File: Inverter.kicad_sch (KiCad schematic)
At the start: 53 parts, among them IC1 STGIPQ3H60T-HL, IC2 ACS724LLCTR-05AU-T

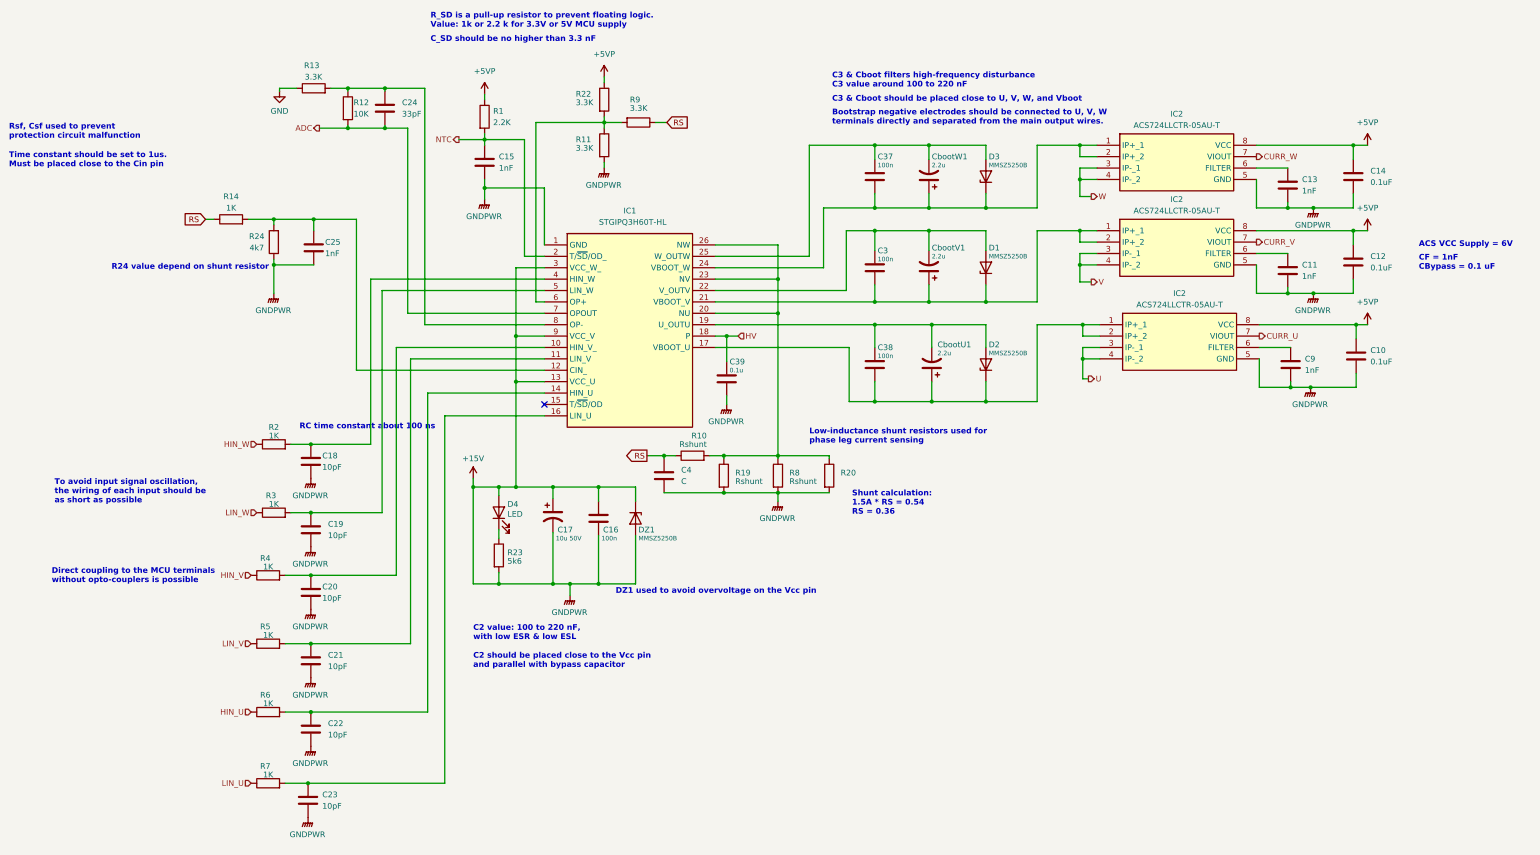
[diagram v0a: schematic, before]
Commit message: add overcurrent protection
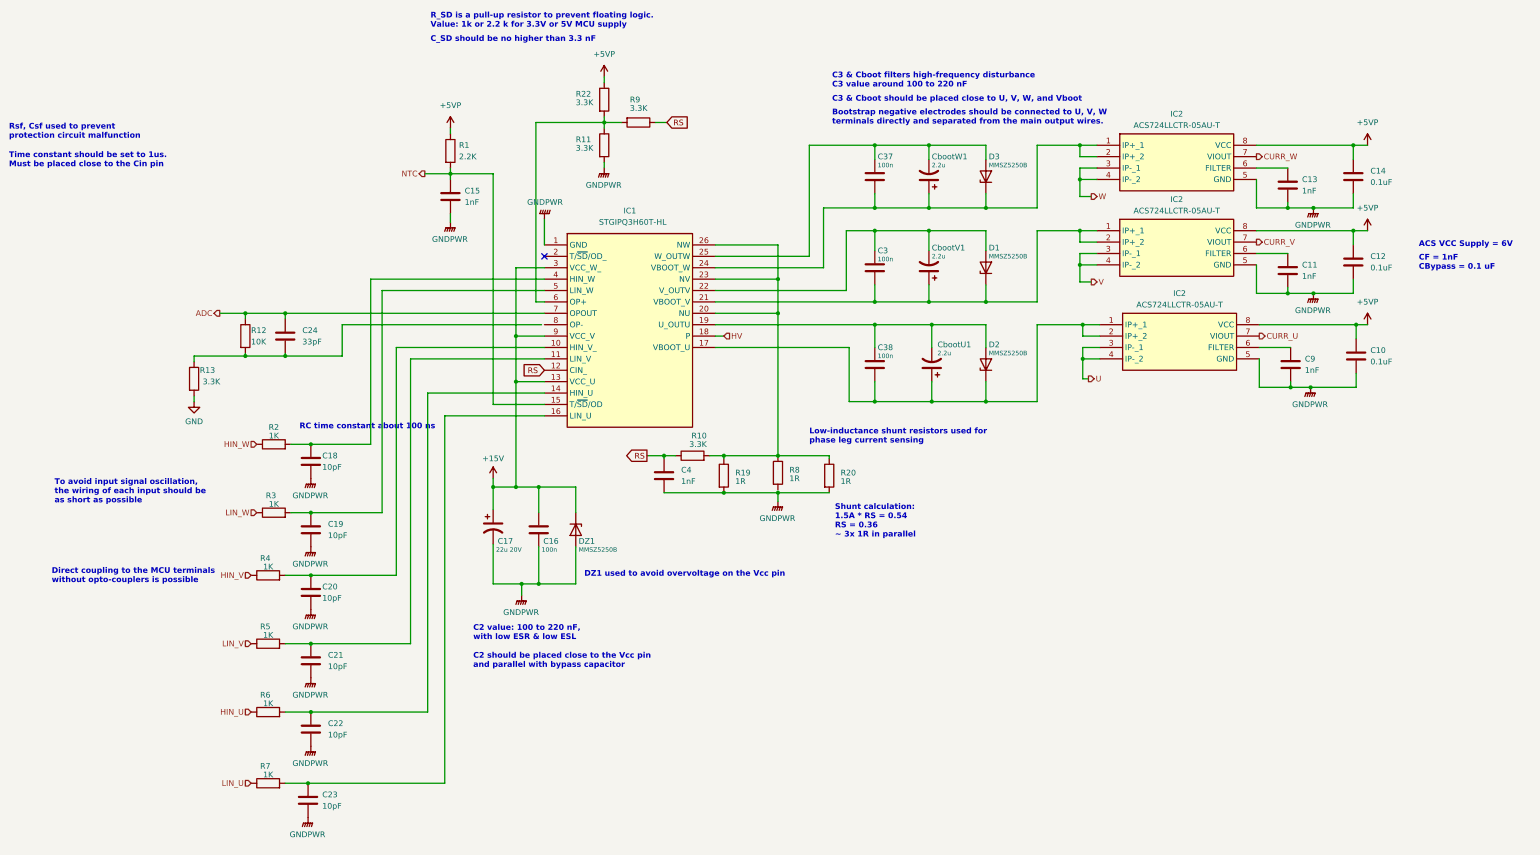
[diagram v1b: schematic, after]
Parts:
- removed C25: 1nF, symbol Device:C
- removed C39: 0.1u, symbol Device:C
- removed D4: LED, LED_THT:LED_D5.0mm, symbol Device:LED
- removed R14: 1K, Resistor_THT:R_Axial_DIN0309_L9.0mm_D3.2mm_P12.70mm_Horizontal, symbol Device:R
- removed R23: 5k6, Resistor_THT:R_Axial_DIN0309_L9.0mm_D3.2mm_P12.70mm_Horizontal, symbol Device:R
- removed R24: 4k7, Resistor_THT:R_Axial_DIN0309_L9.0mm_D3.2mm_P12.70mm_Horizontal, symbol Device:R
- C17: value 10u 50V -> 22u 20V
- C4: value C -> 1nF
- R10: value Rshunt -> 3.3K
- R19, R20, R8: value Rshunt -> 1R
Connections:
- net +15V: no longer C10.1, C11.1, C12.1, C13.1, C14.1, C15.2, C16.1, C17.2, C18.2, C19.2, C20.2, C21.2, C22.2, C23.2, C4.2, C9.1, DZ1.2 (A), IC1.1 (GND), IC2.5 (GND), IC2.5 (GND), IC2.5 (GND), R11.2, R19.2, R20.2, R8.2
- net ADC: now also C24.1, R12.1; no longer C24.2, R12.2
- net GND: now also R13.2; no longer R13.1
- net NTC: now also IC1.15 (T/~{SD}/OD); no longer IC1.2 (T/~{SD}/OD_)
- net RS: now also IC1.12 (CIN_)
- new net: C24.2, R12.2, R13.1
- new net GNDPWR: C10.1, C11.1, C12.1, C13.1, C14.1, C15.2, C16.1, C17.2, C18.2, C19.2, C20.2, C21.2, C22.2, C23.2, C4.2, C9.1, DZ1.2 (A), IC1.1 (GND), IC2.5 (GND), IC2.5 (GND), IC2.5 (GND), R11.2, R19.2, R20.2
- now unconnected: IC1.8 (OP-)
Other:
- note added: "Shunt calculation: 1.5A * RS = 0.54 RS = 0.36 ~ 3x 1R in parallel"
- note removed: "R24 value depend on shunt resistor"
- note removed: "Shunt calculation: 1.5A * RS = 0.54 RS = 0.36"
- moved on the sheet: C15, C16, C17, C24, DZ1, R1, R12, R13

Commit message: update schematics
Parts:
- removed C16: 100n, symbol Device:C
- removed C17: 22u 20V, symbol Device:C_Polarized_US
- removed DZ1: MMSZ5250B, symbol Device:D_Zener
- C10, C11, C12, C13, C14, C15, C18, C19, C20, C21, C22, C23, C24, C3, C37, C38, C4, C9: footprint (none) -> Capacitor_THT:C_Disc_D4.3mm_W1.9mm_P5.00mm
- CbootU1, CbootV1, CbootW1: footprint (none) -> Capacitor_THT:CP_Radial_D5.0mm_P2.50mm
- D1, D2, D3: footprint (none) -> Diode_THT:D_A-405_P7.62mm_Horizontal
- IC2: footprint (none) -> SamacSys_Parts:SOIC127P600X175-8N
- R10, R19, R20, R8: footprint (none) -> Resistor_THT:R_Axial_DIN0309_L9.0mm_D3.2mm_P12.70mm_Horizontal
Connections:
- net GNDPWR is gone; now on net GND: C10.1, C11.1, C12.1, C13.1, C14.1, C15.2, C18.2, C19.2, C20.2, C21.2, C22.2, C23.2, C4.2, C9.1, IC1.1 (GND), IC2.5 (GND), IC2.5 (GND), IC2.5 (GND), R11.2, R19.2, R20.2
- net GND: now also R8.2
- net NTC: now also IC1.2 (T/~{SD}/OD_); no longer IC1.15 (T/~{SD}/OD)
- net at C38.2, CbootU1.1, D2.1 (K)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: no longer IC2.1 (IP+_1), IC2.2 (IP+_2)
- net at C38.1, CbootU1.2, D2.2 (A)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: now also IC2.1 (IP+_1), IC2.2 (IP+_2)
- net at C3.2, CbootV1.1, D1.1 (K)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: no longer IC2.1 (IP+_1), IC2.2 (IP+_2)
- net at C3.1, CbootV1.2, D1.2 (A)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: now also IC2.1 (IP+_1), IC2.2 (IP+_2)
- net at C37.2, CbootW1.1, D3.1 (K)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: no longer IC2.1 (IP+_1), IC2.2 (IP+_2)
- net at C37.1, CbootW1.2, D3.2 (A)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: now also IC2.1 (IP+_1), IC2.2 (IP+_2)
- net at C24.2, R12.2, R13.1: now also IC1.8 (OP-)
- net +5VP renamed +5V

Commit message: pcb layout design
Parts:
- C10, C11, C12, C13, C14, C15, C9: footprint Capacitor_THT:C_Disc_D4.3mm_W1.9mm_P5.00mm -> Capacitor_SMD:C_0805_2012Metric
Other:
- note removed: "C2 should be placed close to the Vcc pin and parallel with bypass capacitor"
- note removed: "C2 value: 100 to 220 nF, with low ESR & low ESL"
- note removed: "DZ1 used to avoid overvoltage on the Vcc pin"
- moved on the sheet: C10, C11, C12, C13, C14, C15, C18, C19, C20, C21, C22, C23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
